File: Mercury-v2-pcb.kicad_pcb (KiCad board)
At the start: 2 copper layers, 72.8 x 100 mm, 147 parts, among them J1 Micro_SD_Card_Det2, J2 UART, J3 Conn_ARM_JTAG_SWD_10, J4 2.54mm 02x03, J5 BATTERY, J6 BATTERY, J7 2.54mm 02x03, J8 Conn_01x02, Q1 BSS138, Q2 IRFML8244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

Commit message: feat: improve pcb
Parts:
- moved D15 60.0 mm to (126.5, 58.2), turned to -40 degrees
- moved D23 59.9 mm to (174.6, 93.8), turned to -5 degrees
- moved D14 59.6 mm to (162.8, 59.6), turned to 40 degrees
- moved D24 59.4 mm to (114.2, 93.8), turned to 5 degrees
- moved R24 41.3 mm to (141.1, 53.8), turned to 0 degrees
- moved R25 41.0 mm to (141.1, 50.5), turned to -90 degrees
- moved R29 37.7 mm to (144.3, 57.0), turned to 180 degrees
- moved R48 37.7 mm to (118.1, 76.7), turned to 180 degrees
- moved Q2 37.4 mm to (143.6, 48.5), turned to 90 degrees
- moved U6 34.9 mm to (145.6, 53.2), turned to 0 degrees
- moved Q5 34.3 mm to (121.4, 77.7), turned to -90 degrees
- moved Q3 33.7 mm to (147.6, 57.9), turned to -90 degrees
- moved R26 32.7 mm to (146.9, 49.4), turned to 0 degrees
- moved U13 31.0 mm to (119.4, 72.9), turned to 180 degrees
- moved R27 29.2 mm to (150.1, 55.1), turned to 180 degrees
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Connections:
- U1 pad 10: /ir_sensor/IR_OUT_A -> /ir_sensor2/IR_OUT_A
- U1 pad 14: /ir_sensor2/IR_OUT_A -> /ir_sensor/IR_OUT_A
- U1 pad 15: /ir_led/IR_LED_IN1 -> /mcu/IR_LED1
- U1 pad 16: /ir_led/IR_LED_IN2 -> /ir_led/IR_LED_IN1
- U1 pad 17: /ir_led_single/IR_LED_IN -> /ir_led/IR_LED_IN2
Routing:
- net +BATT: track 103.1 -> 235.1 mm, vias 5 -> 7
- net Net-(D23-K): track 0.00 -> 66.8 mm
- net Net-(D14-K): track 0.00 -> 34.9 mm
- net /ir_sensor2/IR_OUT_B: track 2.27 -> 32.4 mm
- net Net-(D16-K): track 0.00 -> 28.3 mm
- net /mcu/LED5: track 46.5 -> 74.0 mm
- net Net-(D24-K): track 0.00 -> 25.6 mm
- net Net-(D15-K): track 0.00 -> 25.3 mm
- net /ir_sensor2/IR_OUT_A: track 2.29 -> 27.5 mm
- net /mcu/LED2: track 48.3 -> 73.2 mm, vias 0 -> 4
- net /ir_sensor1/IR_OUT_B: track 2.29 -> 26.6 mm
- net Net-(D17-K): track 0.00 -> 20.2 mm, vias 0 -> 1
- net /mcu/LED3: track 70.7 -> 51.2 mm, vias 0 -> 2
- net /ir_sensor/IR_OUT_B: track 2.31 -> 21.6 mm
- net /ir_sensor1/IR_OUT_A: track 2.29 -> 21.0 mm
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
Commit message: feat: route tracks
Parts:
- moved R40 6.88 mm to (161.6, 70.9)
- moved L1 3.55 mm to (159.8, 106.2)
- moved R35 3.55 mm to (159.8, 108.5)
- moved C29 3.55 mm to (159.5, 104.0)
- moved C30 3.55 mm to (161.3, 101.2)
- moved R36 3.55 mm to (158.6, 101.7)
- moved R37 3.55 mm to (160.1, 101.7)
- moved D20 2.59 mm to (160.4, 66.6), turned to -70 degrees
- moved D5 1.74 mm to (164.3, 71.1)
- moved R10 1.74 mm to (164.3, 72.7)
- moved D7 1.03 mm to (127.3, 71.1)
- moved R13 1.03 mm to (127.3, 72.8)
- moved R32 0.98 mm to (156.1, 112.4)
- moved R31 0.98 mm to (156.7, 113.1)
- moved J2 0.58 mm to (125.0, 122.0)
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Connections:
- D12 pad 2: Net-(C13-Pad2) -> Net-(C15-Pad2)
- D13 pad 2: Net-(C15-Pad2) -> Net-(C13-Pad2)
- D19 pad 2: Net-(C31-Pad2) -> Net-(C33-Pad2)
- D20 pad 2: Net-(C33-Pad2) -> Net-(C31-Pad2)
- D21 pad 2: Net-(C35-Pad2) -> Net-(C37-Pad2)
- D22 pad 2: Net-(C37-Pad2) -> Net-(C35-Pad2)
- R20 pad 1: Net-(C13-Pad2) -> Net-(C15-Pad2)
- R22 pad 1: Net-(C15-Pad2) -> Net-(C13-Pad2)
- R38 pad 1: Net-(C31-Pad2) -> Net-(C33-Pad2)
- R40 pad 1: Net-(C33-Pad2) -> Net-(C31-Pad2)
- R42 pad 1: Net-(C35-Pad2) -> Net-(C37-Pad2)
- R44 pad 1: Net-(C37-Pad2) -> Net-(C35-Pad2)
- U1 pad 15: /mcu/IR_LED1 -> /ir_led/IR_LED_IN2
- U1 pad 17: /ir_led/IR_LED_IN2 -> /ir_led_single/IR_LED_IN
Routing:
- net +3.3VADC: track 5.79 -> 262.1 mm, vias 0 -> 6
- net +3.3V: track 37.9 -> 242.3 mm, vias 0 -> 11
- net /ir_led/IR_LED_IN1: track 1.69 -> 84.0 mm, vias 0 -> 3
- net /ir_led/IR_LED_IN2: track 1.69 -> 75.3 mm, vias 0 -> 2
- net /ir_led_single/IR_LED_IN: track 1.68 -> 58.7 mm, vias 0 -> 2
- net Net-(C13-Pad2): track 2.53 -> 51.2 mm, vias 0 -> 2
- net /mcu/ACS_IN_R: track 3.02 -> 51.5 mm, vias 0 -> 2
- net /mcu/ACS_IN_L: track 2.48 -> 50.0 mm, vias 0 -> 2
- net Net-(C35-Pad2): track 2.19 -> 46.5 mm, vias 0 -> 1
- net Net-(C15-Pad2): track 2.18 -> 46.1 mm, vias 0 -> 2
- net Net-(C37-Pad2): track 2.38 -> 41.0 mm, vias 0 -> 1
- net Net-(C33-Pad2): track 2.61 -> 40.8 mm, vias 0 -> 1
- net Net-(C31-Pad2): track 2.56 -> 37.1 mm, vias 0 -> 1
- net +1.65VADC: track 17.5 -> 46.0 mm, vias 0 -> 5
- net /mcu/LED5: track 74.0 -> 97.4 mm
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
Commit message: feat: add filled zone
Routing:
- added copper zone on B.Cu, net (none)
- added copper zone on F.Cu, net (none)
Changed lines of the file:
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@@
+	)
+	(zone
+		(net 0)
+		(net_name "")
+		(layers "F&B.Cu")
+		(name "GND_zone")
+		(hatch edge 0.5)
+		(priority 1)
+		(connect_pads
+			(clearance 0.508)
+		)
+		(min_thickness 0.25)
+		(filled_areas_thickness no)
+		(fill yes
+			(thermal_gap 0.5)
+			(thermal_bridge_width 0.5)
+			(island_removal_mode 1)
+			(island_area_min 10)
+		)
+		(polygon
+			(pts
+				(xy 173.34 146.7) (xy 98 146.36) (xy 100.66 37.03) (xy 191.39 38.58) (xy 185.66 146.52)
+			)
+		)
 	)
 	(zone
@@
 		(net_name "+BATT")
 		(layer "B.Cu")
+		(name "BATT_zone")
 		(hatch edge 0.5)
+		(priority 2)
 		(connect_pads
 			(clearance 0.508)

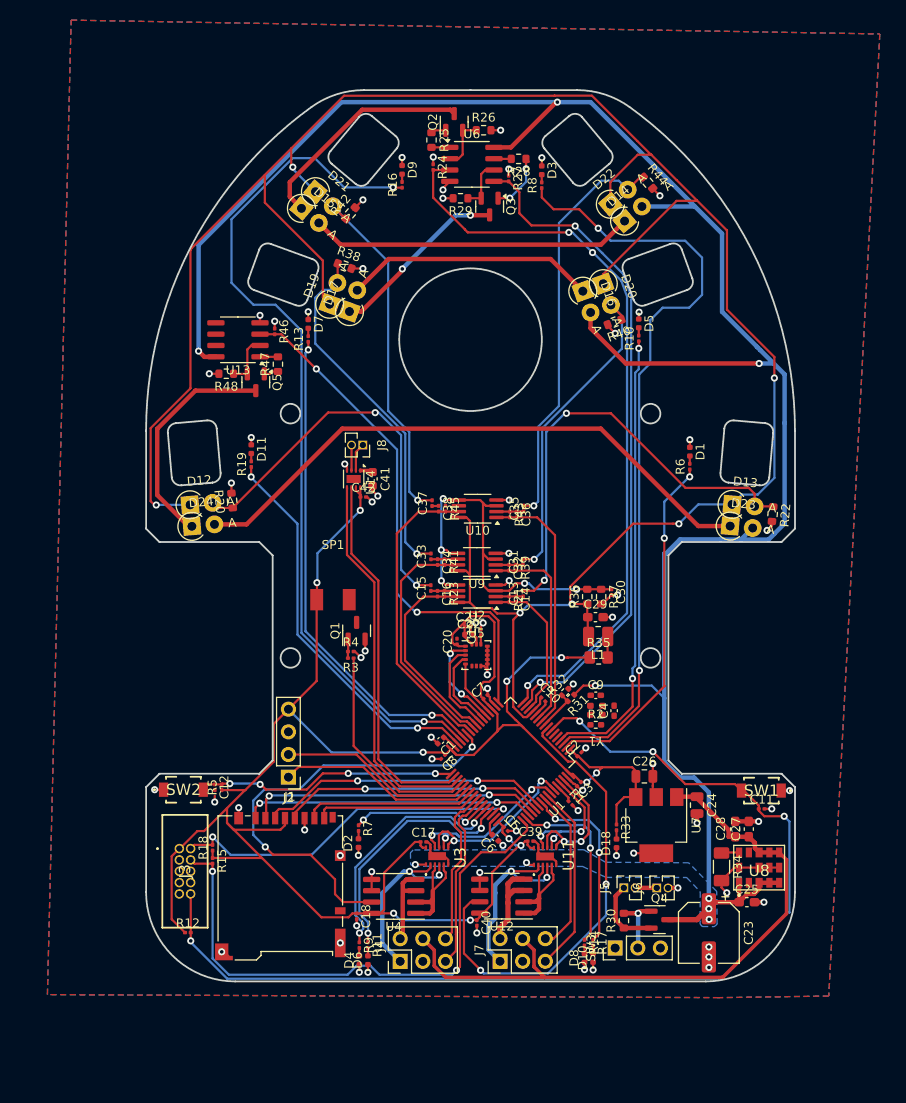
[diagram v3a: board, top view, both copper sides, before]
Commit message: feat: finish zone and via
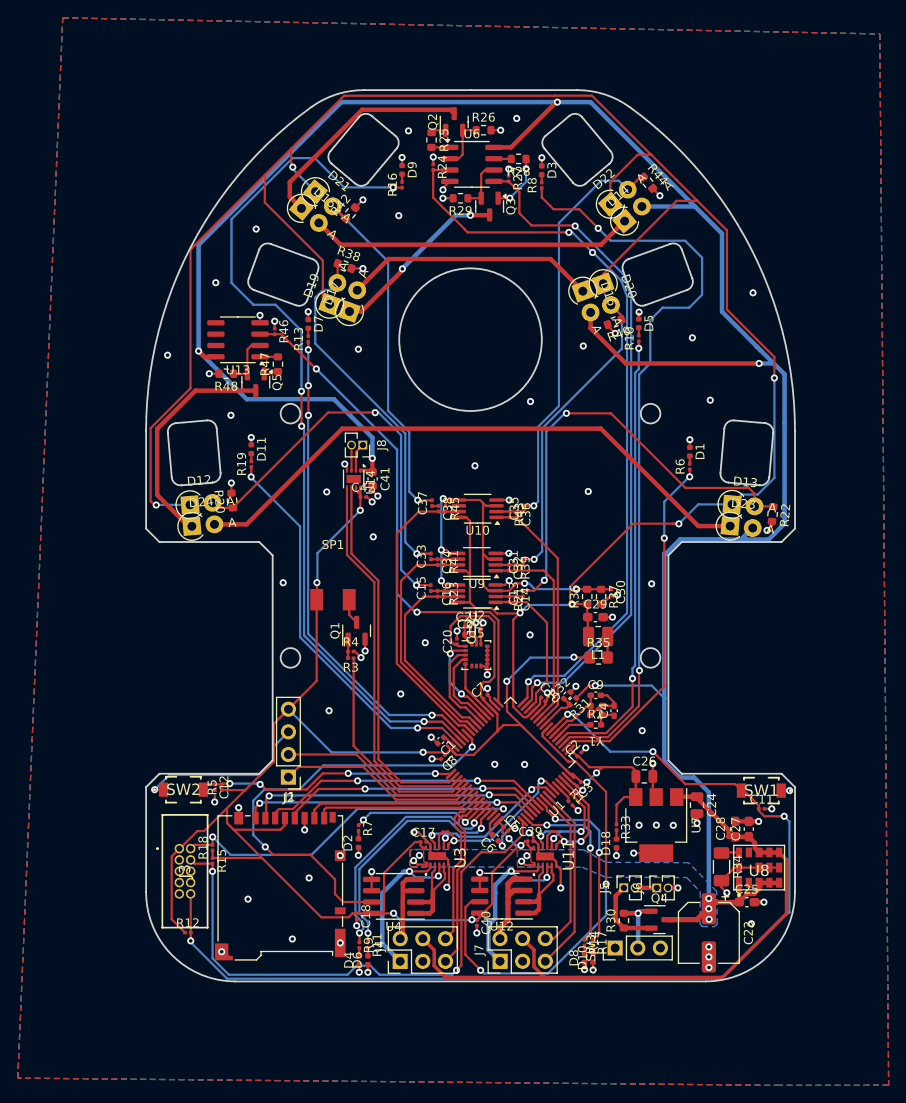
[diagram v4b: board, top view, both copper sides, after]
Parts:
- moved R31 0.44 mm to (157.0, 113.5)
- moved R32 0.44 mm to (156.3, 112.8)
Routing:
- net GND: track 102.1 -> 139.6 mm, vias 71 -> 110
- net +BATT: track 250.3 -> 278.6 mm, vias 9 -> 12
- net /mcu/OSC_OUT: track 0.00 -> 6.56 mm
- net /mcu/OSC_IN: track 0.00 -> 4.28 mm
- net Net-(Q1-D): track 0.00 -> 2.90 mm
- net Net-(C4-Pad1): track 0.00 -> 2.55 mm
- net +3.3V: track 242.3 -> 244.0 mm
- net /ir_sensor2/IR_OUT_A: track 28.9 -> 27.8 mm
- net /mcu/LED4: track 55.2 -> 55.0 mm, vias 2 -> 4
- net /mcu/LED5: vias 2 -> 4
- added copper zone on F.Cu, net +BATT
- added copper zone on B.Cu, net GND
- added copper zone on F.Cu, net GND
- removed copper zone on B.Cu, net (none)
- removed copper zone on F.Cu, net (none)
